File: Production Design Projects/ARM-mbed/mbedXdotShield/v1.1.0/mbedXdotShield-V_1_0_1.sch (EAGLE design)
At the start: 70 parts, among them CON1 47346-0001, CON2 S2B-PH-SM4-TB(LF)(SN), Q1 12MHz, SW3 JS202011JCQN, T1 BSS84, U1 MTXDOT-EU1-A00-1, U2 TLV73333PDBVT, U3 AT45DB321E-SHF-B

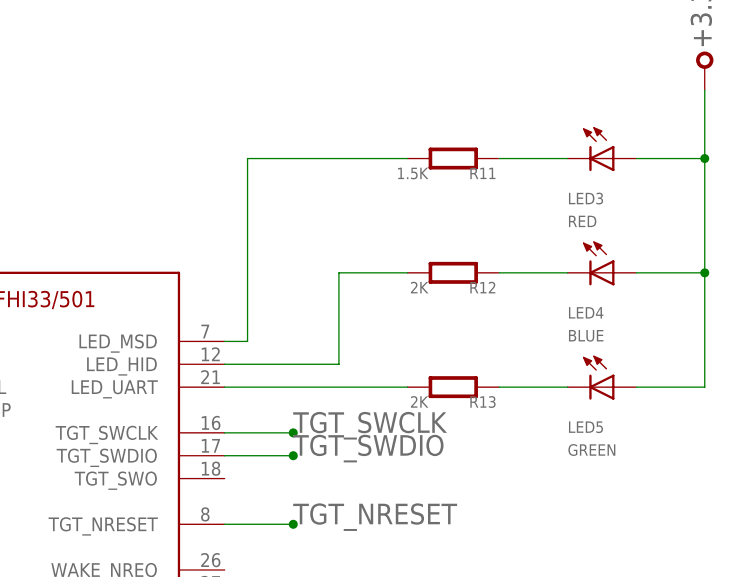
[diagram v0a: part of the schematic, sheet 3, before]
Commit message: Added v1.1.0 updated schematic. R3:1.5K->220R, R13,R14:470R->1.5K, rerouted UART1_, moved USB micro into board, placed resistors R14-to-R27 on front of PCB (no components on rear)
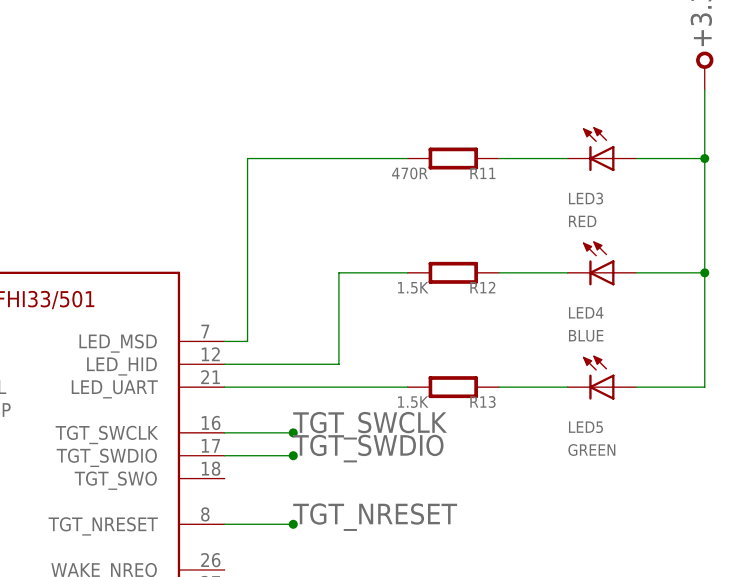
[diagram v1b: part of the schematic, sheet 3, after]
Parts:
- R11: value 1.5K -> 470R
- R12, R13: value 2K -> 1.5K
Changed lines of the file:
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@@
 <part name="R8" library="mbed-HDK-RLCQ" deviceset="RESISTOR" device="0402" value="1.5K"/>
 <part name="R10" library="mbed-HDK-RLCQ" deviceset="RESISTOR" device="0402" value="10K"/>
-<part name="R11" library="mbed-HDK-RLCQ" deviceset="RESISTOR" device="0402" value="1.5K"/>
-<part name="R12" library="mbed-HDK-RLCQ" deviceset="RESISTOR" device="0402" value="2K"/>
-<part name="R13" library="mbed-HDK-RLCQ" deviceset="RESISTOR" device="0402" value="2K"/>
+<part name="R11" library="mbed-HDK-RLCQ" deviceset="RESISTOR" device="0402" value="470R"/>
+<part name="R12" library="mbed-HDK-RLCQ" deviceset="RESISTOR" device="0402" value="1.5K"/>
+<part name="R13" library="mbed-HDK-RLCQ" deviceset="RESISTOR" device="0402" value="1.5K"/>
 <part name="R9" library="mbed-HDK-RLCQ" deviceset="RESISTOR" device="0402" value="10K"/>
 <part name="LED3" library="mbed-HDK-Optical" deviceset="SMD_LED" device="0603" value="RED"/>
